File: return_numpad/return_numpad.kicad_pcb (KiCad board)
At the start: 2 copper layers, 33 parts, among them SW1 SW_Push, SW10 SW_Push, SW11 SW_Push, SW12 SW_Push, SW13 SW_Push, SW14 SW_Push, SW15 SW_Push, SW16 SW_Push, SW2 SW_Push, SW3 SW_Push, SW4 SW_Push, SW5 SW_Push, SW6 SW_Push, SW7 SW_Push, SW8 SW_Push, SW9 SW_Push

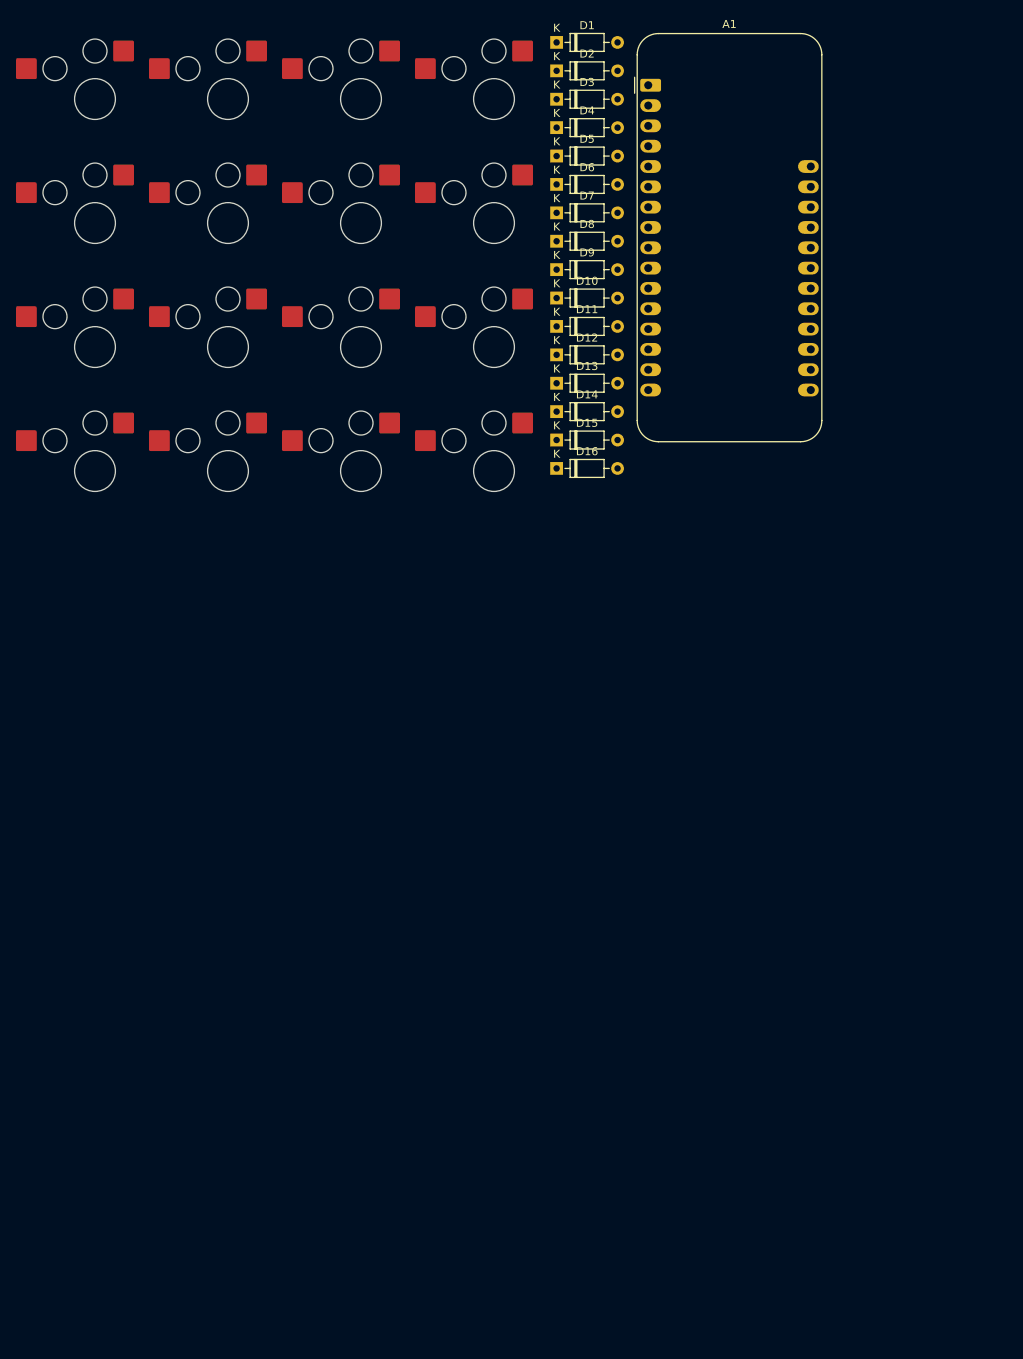
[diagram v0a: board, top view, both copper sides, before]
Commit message: Finish main schematic, finish aux schematic, add production files.
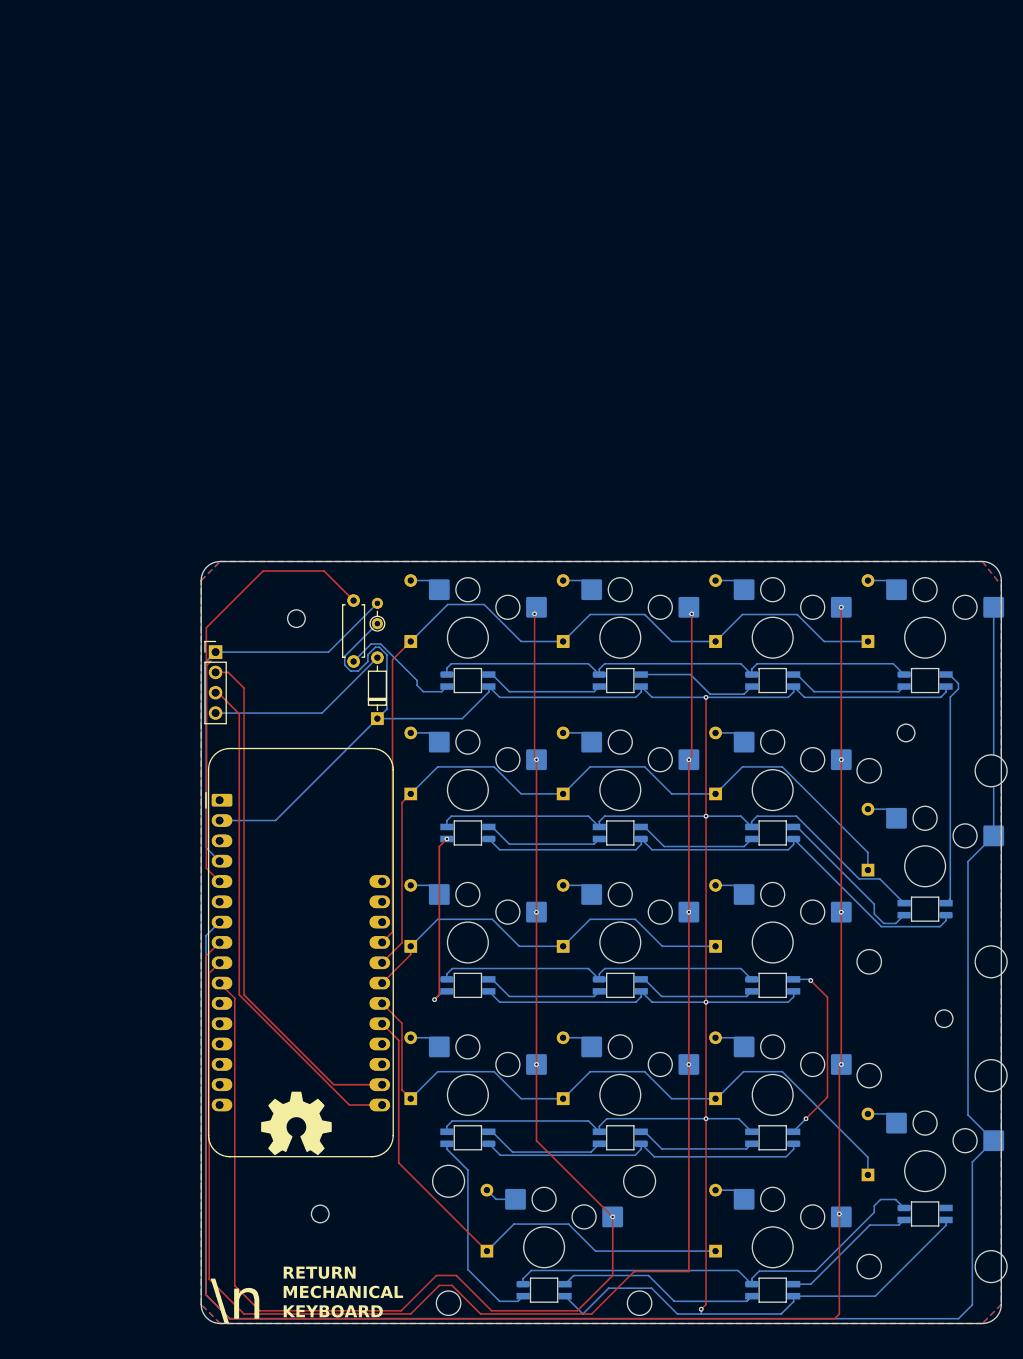
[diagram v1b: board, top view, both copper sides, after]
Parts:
- removed SW12: SW_Push, Kailh_PG1353_Hotswap:Kailh-PG1353-Hotswap-1U
- added C1: 1000uF, Resistor_THT:R_Axial_DIN0204_L3.6mm_D1.6mm_P2.54mm_Vertical, F.Cu at (45.8, 7.77)
- added D17: D_Small, Diode_THT:D_DO-35_SOD27_P7.62mm_Horizontal, B.Cu at (59.5, 86.2)
- added D18: D_Small, Diode_THT:D_DO-35_SOD27_P7.62mm_Horizontal, F.Cu at (45.8, 19.6)
- added D19: D_Small, Diode_THT:D_DO-35_SOD27_P7.62mm_Horizontal, B.Cu at (88.1, 86.2)
- added D21: SK6812MINI, Keebio-Parts:SK6812-MINI-E, F.Cu at (57.2, 14.9)
- added D22: SK6812MINI, Keebio-Parts:SK6812-MINI-E, F.Cu at (76.2, 14.9)
- added D23: SK6812MINI, Keebio-Parts:SK6812-MINI-E, F.Cu at (95.3, 14.9)
- added D24: SK6812MINI, Keebio-Parts:SK6812-MINI-E, F.Cu at (114.3, 14.9)
- added D25: SK6812MINI, Keebio-Parts:SK6812-MINI-E, F.Cu at (114.3, 43.5)
- added D26: SK6812MINI, Keebio-Parts:SK6812-MINI-E, F.Cu at (95.3, 33.9)
- added D27: SK6812MINI, Keebio-Parts:SK6812-MINI-E, F.Cu at (76.2, 33.9)
- added D28: SK6812MINI, Keebio-Parts:SK6812-MINI-E, F.Cu at (57.2, 33.9)
- added D29: SK6812MINI, Keebio-Parts:SK6812-MINI-E, F.Cu at (57.2, 53.0)
- added D30: SK6812MINI, Keebio-Parts:SK6812-MINI-E, F.Cu at (76.2, 53.0)
- added D31: SK6812MINI, Keebio-Parts:SK6812-MINI-E, F.Cu at (95.3, 53.0)
- added D32: SK6812MINI, Keebio-Parts:SK6812-MINI-E, F.Cu at (95.3, 72.0)
- added D33: SK6812MINI, Keebio-Parts:SK6812-MINI-E, F.Cu at (76.2, 72.0)
- added D34: SK6812MINI, Keebio-Parts:SK6812-MINI-E, F.Cu at (57.2, 72.0)
- added D35: SK6812MINI, Keebio-Parts:SK6812-MINI-E, F.Cu at (66.7, 91.1)
- added D36: SK6812MINI, Keebio-Parts:SK6812-MINI-E, F.Cu at (95.3, 91.1)
- added G***: LOGO, LOGO, F.Cu at (73.8, 46.4)
- added G***: LOGO, LOGO, F.Cu at (35.7, 70.2)
- added J1: Conn_01x04, Connector_PinHeader_2.54mm:PinHeader_1x04_P2.54mm_Vertical, F.Cu at (25.6, 11.3)
- added R1: 500, Resistor_THT:R_Axial_DIN0207_L6.3mm_D2.5mm_P7.62mm_Horizontal, F.Cu at (42.9, 4.88)
- added REF**: MountingHole_2.2mm_M2, MountingHole:MountingHole_2.2mm_M2, F.Cu at (38.7, 81.6)
- added REF**: MountingHole_2.2mm_M2, MountingHole:MountingHole_2.2mm_M2, F.Cu at (116.7, 57.2)
- added REF**: 2U, Alps_MX_Stabilizers:Alps-MX-Stabilizers-2U, F.Cu at (66.7, 85.7)
- added REF**: MountingHole_2.2mm_M2, MountingHole:MountingHole_2.2mm_M2, F.Cu at (111.9, 21.4)
- added REF**: 2U-Vertical, Alps_MX_Stabilizers:Alps-MX-Stabilizers-2U-Vertical, F.Cu at (114.3, 38.1)
- added REF**: MountingHole_2.2mm_M2, MountingHole:MountingHole_2.2mm_M2, F.Cu at (35.7, 7.14)
- added REF**: 2U-Vertical, Alps_MX_Stabilizers:Alps-MX-Stabilizers-2U-Vertical, F.Cu at (114.3, 76.2)
- added SW17: SW_Push, Kailh_PG1353_Hotswap:Kailh-PG1353-Hotswap-1U, B.Cu at (66.7, 85.7)
- added SW19: SW_Push, Kailh_PG1353_Hotswap:Kailh-PG1353-Hotswap-1U, B.Cu at (95.3, 85.7)
- D1, D10, D11, D13, D14, D15, D16, D2, D3, D4, D5, D6, D7, D8, D9, SW1, SW10, SW11, SW13, SW14, SW15, SW16, SW2, SW3, SW4, SW5, SW6, SW7, SW8, SW9: moved to B.Cu
- D12: value D_Small -> SK6812MINI; footprint Diode_THT:D_DO-35_SOD27_P7.62mm_Horizontal -> Keebio-Parts:SK6812-MINI-E
- moved SW13 124.5 mm to (57.2, 66.7), turned to 180 degrees
- moved D12 116.9 mm to (114.3, 81.6), turned to 180 degrees
- moved SW14 110.1 mm to (76.2, 66.7), turned to 180 degrees
- moved SW9 106.3 mm to (57.2, 47.6), turned to 180 degrees
- moved SW4 105.8 mm to (114.3, 9.53), turned to 180 degrees
- moved A1 104.2 mm to (26.1, 29.8)
- moved SW16 102.8 mm to (114.3, 76.2), turned to 180 degrees
- moved SW8 100.2 mm to (114.3, 38.1), turned to 180 degrees
- moved SW15 99.8 mm to (95.3, 66.7), turned to 180 degrees
- moved D16 96.5 mm to (107.2, 76.7), turned to 90 degrees
- moved SW10 95.6 mm to (76.2, 47.6), turned to 180 degrees
- moved SW3 92.2 mm to (95.3, 9.53), turned to 180 degrees
- moved SW5 91.4 mm to (57.2, 28.6), turned to 180 degrees
- moved D13 91.3 mm to (50.0, 67.2), turned to 90 degrees
- moved SW11 90.5 mm to (95.3, 47.6), turned to 180 degrees
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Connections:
- A1 pad 10: unconnected-(A1-A5-Pad10) -> COL0
- A1 pad 2: unconnected-(A1-3V3-Pad2) -> +3.3V
- A1 pad 21: unconnected-(A1-D2-Pad21) -> ROW4
- A1 pad 22: unconnected-(A1-D3-Pad22) -> ROW3
- A1 pad 23: unconnected-(A1-D4-Pad23) -> ROW2
- A1 pad 24: unconnected-(A1-D5-Pad24) -> ROW1
- A1 pad 25: unconnected-(A1-D6-Pad25) -> ROW0
- A1 pad 4: unconnected-(A1-GND-Pad4) -> GND
- A1 pad 5: unconnected-(A1-A0-Pad5) -> LED_DIN
- A1 pad 7: unconnected-(A1-A2-Pad7) -> COL3
- A1 pad 8: unconnected-(A1-A3-Pad8) -> COL2
- A1 pad 9: unconnected-(A1-A4-Pad9) -> COL1
- D12 pad 1: ROW2 -> unconnected-(D12-DOUT-Pad1)
- D12 pad 2: Net-(D12-A) -> GND
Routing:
- net +3.3V: track 0.00 -> 408.2 mm, vias 0 -> 5
- net GND: track 0.00 -> 315.2 mm
- net COL3: track 0.00 -> 236.0 mm
- net COL2: track 0.00 -> 214.3 mm, vias 0 -> 5
- net COL1: track 0.00 -> 190.3 mm, vias 0 -> 4
- net COL0: track 0.00 -> 180.3 mm, vias 0 -> 5
- net ROW0: track 0.00 -> 105.7 mm
- net ROW1: track 0.00 -> 93.4 mm
- net ROW3: track 0.00 -> 84.2 mm
- net ROW4: track 0.00 -> 65.2 mm
- net Net-(A1-SCL): track 0.00 -> 64.6 mm
- net Net-(A1-SDA): track 0.00 -> 62.7 mm
- net LED_DIN: track 0.00 -> 56.1 mm
- net ROW2: track 0.00 -> 49.8 mm
- net Net-(D24-DOUT): track 0.00 -> 30.1 mm
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- added copper zone on B.Cu, net GND
- added copper zone on F.Cu, net GND
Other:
- board outline added: 100 x 95.3 mm
- board text added: "RETURN MECHANICAL KEYBOARD"
- board text added: "\n"
